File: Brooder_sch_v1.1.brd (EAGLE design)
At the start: 80 x 75 mm, 28 parts, among them J1 DCJ0202, U1 328P

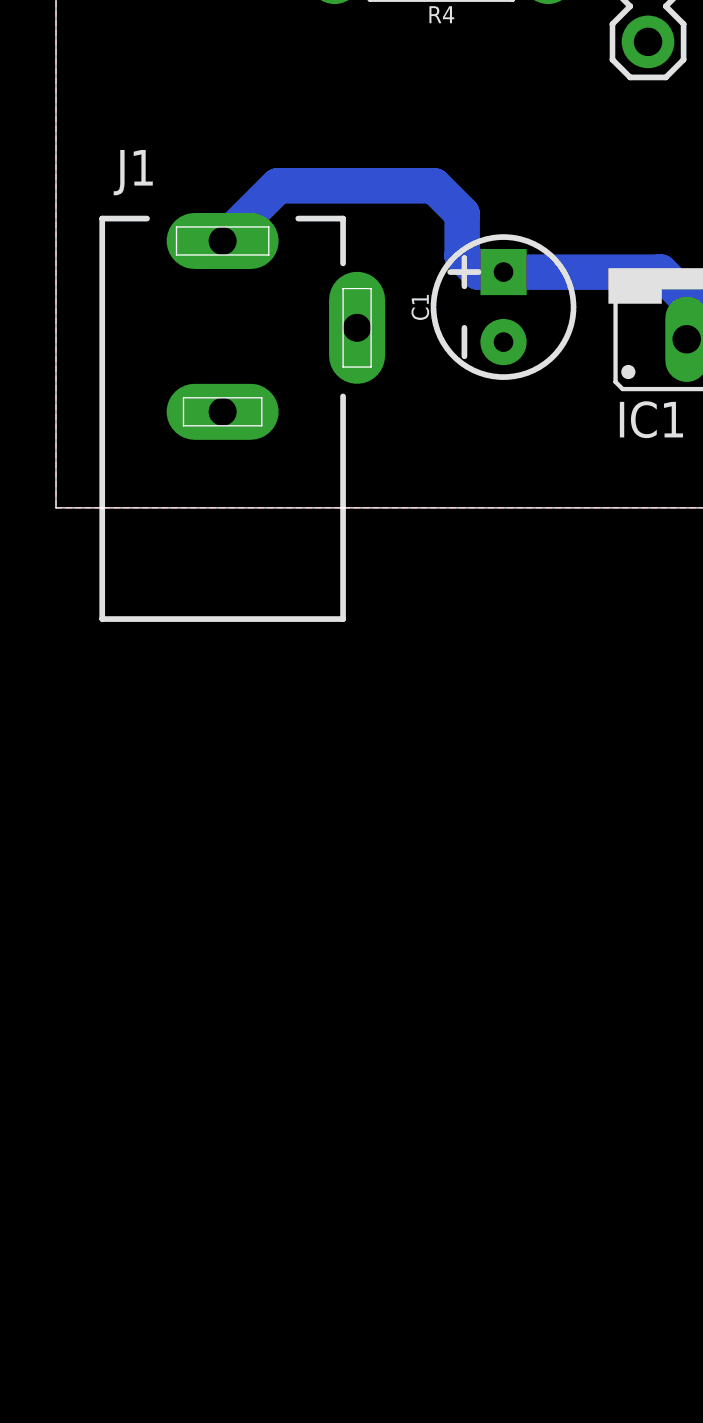
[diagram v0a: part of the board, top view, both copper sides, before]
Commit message: Adds space for the rocker switch
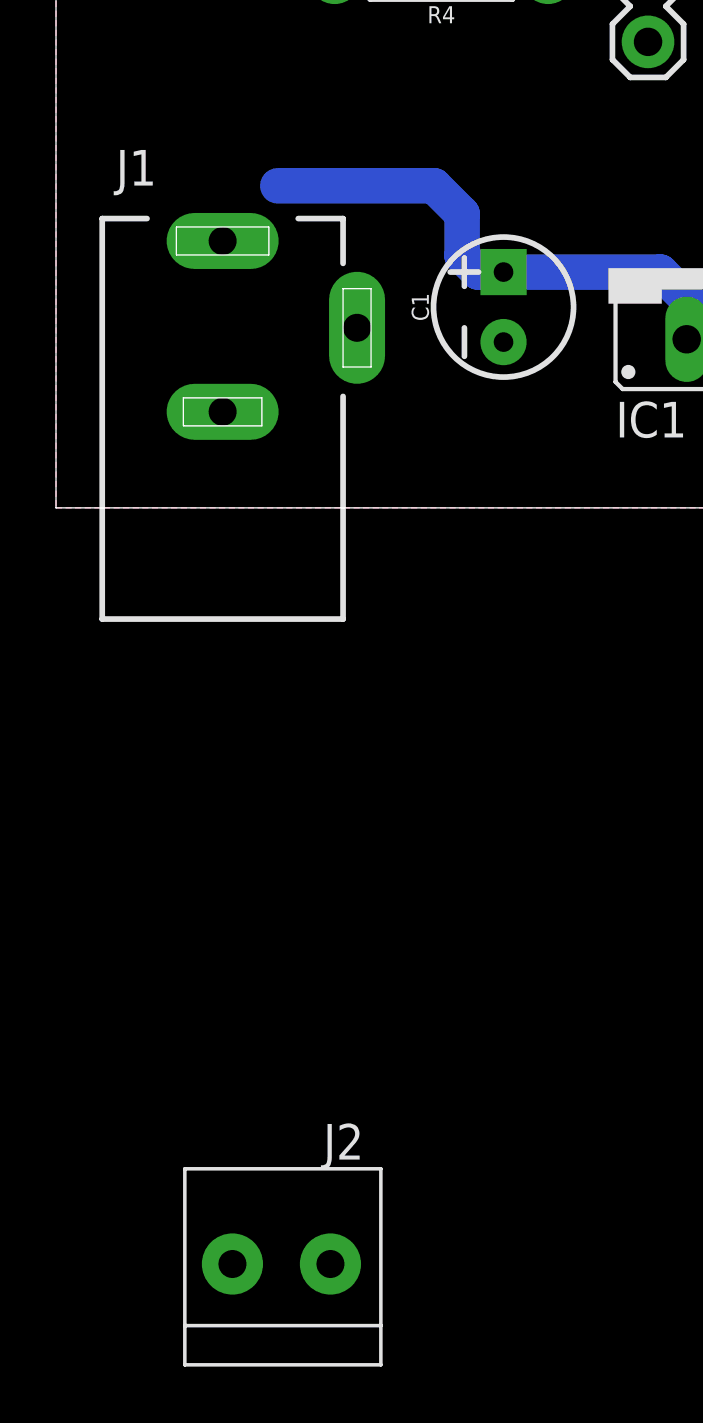
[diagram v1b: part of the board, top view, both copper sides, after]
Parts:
- added J2: 1X2-3.5MM, adafruit:1X2-3.5MM
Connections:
- new net 12V_S: C1.1, IC1.IN, J2.2
- net 12V: now also J2.1; no longer C1.1, IC1.IN
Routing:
- net 12V: track 21.4 -> 0.00 mm
- net 12V_S: track 0.00 -> 18.6 mm
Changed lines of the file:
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@@
 <attribute name="PROD_ID" value="IC-09136" x="38.13" y="40.02" size="1.778" layer="27" rot="R270" display="off"/>
 </element>
+<element name="J2" library="adafruit" package="1X2-3.5MM" value="1X2-3.5MM" x="8" y="-27"/>
 </elements>
 <signals>
@@
 <signal name="12V">
 <contactref element="J1" pad="1"/>
-<contactref element="C1" pad="1"/>
-<contactref element="IC1" pad="IN"/>
-<wire x1="5.95" y1="9.53" x2="7.92" y2="11.5" width="1.27" layer="16"/>
-<wire x1="7.92" y1="11.5" x2="13.5" y2="11.5" width="1.27" layer="16"/>
-<wire x1="13.5" y1="11.5" x2="14.5" y2="10.5" width="1.27" layer="16"/>
-<wire x1="14.5" y1="10.5" x2="14.5" y2="9" width="1.27" layer="16"/>
-<wire x1="14.5" y1="9" x2="15.08" y2="8.42" width="1.27" layer="16"/>
-<wire x1="15.08" y1="8.42" x2="15.98" y2="8.42" width="1.27" layer="16"/>
-<wire x1="15.98" y1="8.42" x2="21.58" y2="8.42" width="1.27" layer="16"/>
-<wire x1="22.52" y1="7.48" x2="22.52" y2="6.02" width="1.27" layer="16"/>
-<wire x1="21.58" y1="8.42" x2="22.52" y2="7.48" width="1.27" layer="16"/>
+<contactref element="J2" pad="1"/>
+<wire x1="5.95" y1="9.53" x2="9.8" y2="-27" width="0" layer="19" extent="1-1"/>
 </signal>
 <signal name="5V">
@@
 <wire x1="41.99" y1="26" x2="41.94" y2="26.05" width="1.27" layer="16"/>
 </signal>
+<signal name="12V_S">
+<contactref element="C1" pad="1"/>
+<contactref element="IC1" pad="IN"/>
+<contactref element="J2" pad="2"/>
+<wire x1="7.92" y1="11.5" x2="13.5" y2="11.5" width="1.27" layer="16"/>
+<wire x1="13.5" y1="11.5" x2="14.5" y2="10.5" width="1.27" layer="16"/>
+<wire x1="14.5" y1="10.5" x2="14.5" y2="9" width="1.27" layer="16"/>
+<wire x1="14.5" y1="9" x2="15.08" y2="8.42" width="1.27" layer="16"/>
+<wire x1="15.08" y1="8.42" x2="15.98" y2="8.42" width="1.27" layer="16"/>
+<wire x1="15.98" y1="8.42" x2="21.58" y2="8.42" width="1.27" layer="16"/>
+<wire x1="22.52" y1="7.48" x2="22.52" y2="6.02" width="1.27" layer="16"/>
+<wire x1="21.58" y1="8.42" x2="22.52" y2="7.48" width="1.27" layer="16"/>
+<wire x1="15.08" y1="8.42" x2="6.3" y2="-27" width="0" layer="19" extent="16-16"/>
+</signal>
 </signals>

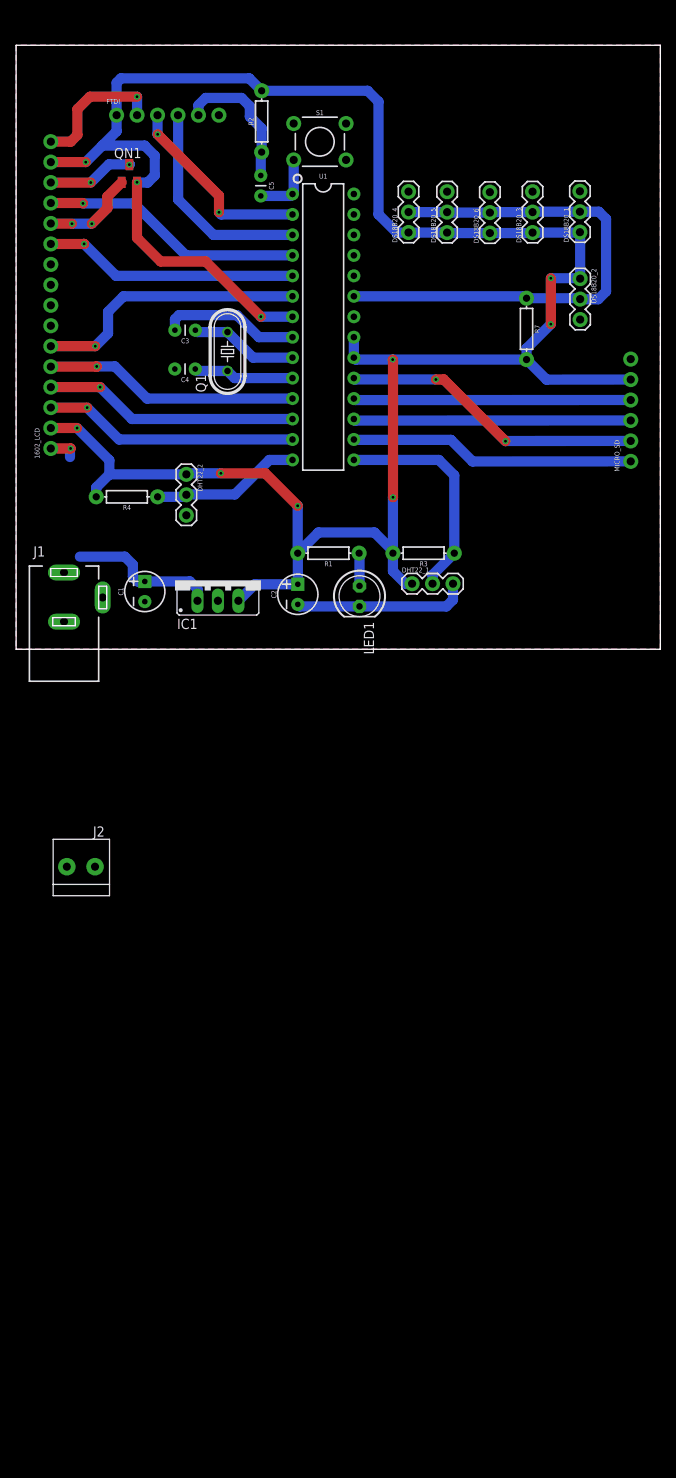
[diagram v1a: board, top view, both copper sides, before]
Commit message: Resolves inconsistencies between the board and schematic
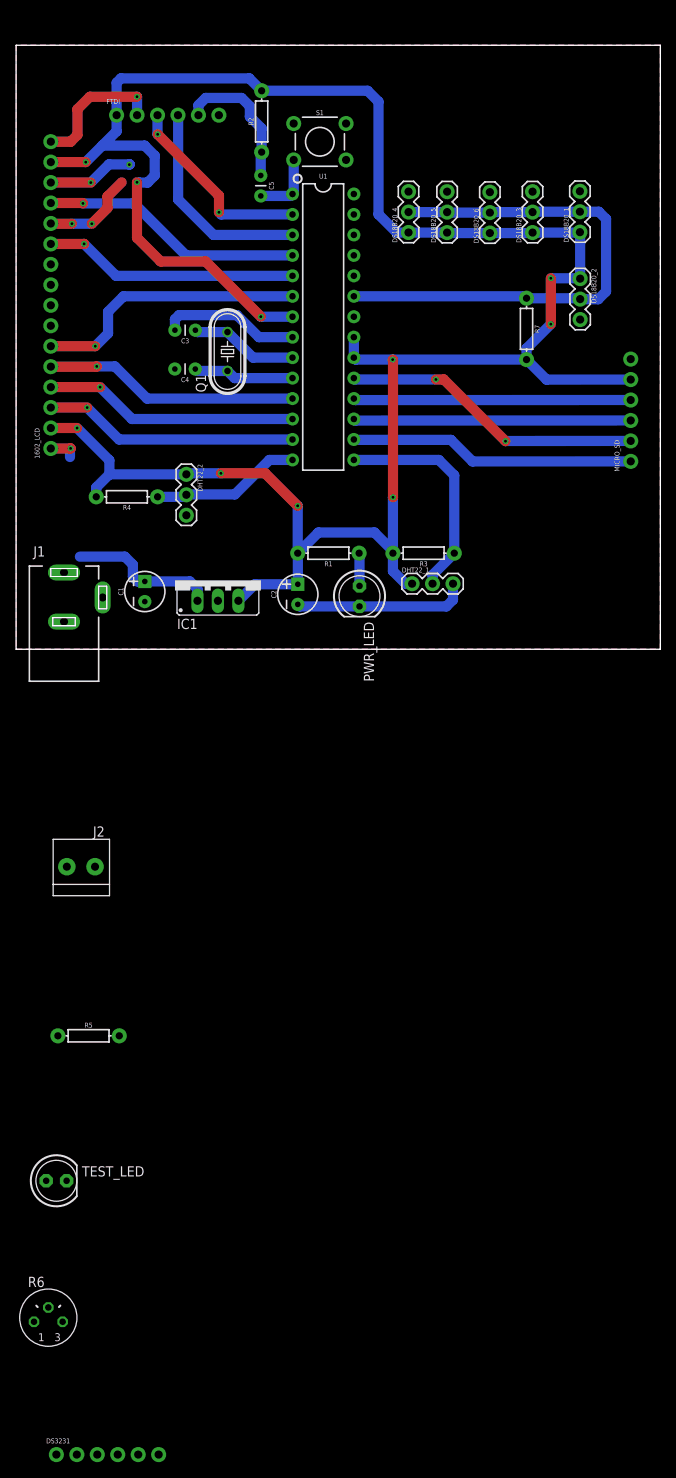
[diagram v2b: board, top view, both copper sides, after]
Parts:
- removed QN1: (no value), sym:SOT23
- added DS3231: (no value), SparkFun-Connectors:1X06_NO_SILK
- added R5: 220, SparkFun-Resistors:AXIAL-0.3
- added R6: (no value), pot:RJ6
- added TEST_LED: (no value), adafruit:LED5MM
- renumbered LED1 to PWR_LED
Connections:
- new net N$1: R5.P$1, TEST_LED.A
- new net PC1: R5.P$2, U1.24
- new net PC4: DS3231.4, U1.27
- new net PC5: DS3231.3, U1.28
- net 5V: now also DS3231.5, R6.E; no longer QN1.2
- net GND: now also DS3231.6, R6.A, TEST_LED.K; no longer QN1.1
- net VO: now also R6.S; no longer QN1.3
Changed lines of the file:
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@@
 <attribute name="OC_NEWARK" value="unknown" x="5.95" y="6.43" size="1.778" layer="27" display="off"/>
 </element>
-<element name="LED1" library="adafruit" package="LED5MM" value="" x="42.64" y="6.59" rot="R270"/>
+<element name="PWR_LED" library="adafruit" package="LED5MM" value="" x="42.64" y="6.59" rot="R270"/>
 <element name="MICRO_SD" library="SparkFun-Connectors" package="1X06_NO_SILK" value="" x="76.32" y="23.33" rot="R90">
 <attribute name="PROD_ID" value="CONN-08437" x="76.32" y="23.33" size="1.778" layer="27" rot="R90" display="off"/>
@@
 <attribute name="OC_NEWARK" value="unknown" x="26.25" y="36.97" size="1.778" layer="27" rot="R90" display="off"/>
 </element>
-<element name="QN1" library="sym" package="SOT23" value="" x="14.06" y="59.08"/>
 <element name="R1" library="SparkFun-Resistors" package="AXIAL-0.3" value="220" x="38.78" y="11.93" rot="R180">
 <attribute name="PROD_ID" value="RES-09327" x="38.78" y="11.93" size="1.778" layer="27" rot="R180" display="off"/>
@@
 </element>
 <element name="J2" library="adafruit" package="1X2-3.5MM" value="1X2-3.5MM" x="8" y="-27"/>
+<element name="R5" library="SparkFun-Resistors" package="AXIAL-0.3" value="220" x="9" y="-48">
+<attribute name="PROD_ID" value="RES-09327" x="9" y="-48" size="1.778" layer="27" display="off"/>
+</element>
+<element name="TEST_LED" library="adafruit" package="LED5MM" value="" x="5" y="-66"/>
+<element name="R6" library="pot" library_urn="urn:adsk.eagle:library:331" package="RJ6" package3d_urn="urn:adsk.eagle:package:22699/1" value="" x="4" y="-83"/>
+<element name="DS3231" library="SparkFun-Connectors" package="1X06_NO_SILK" value="" x="5" y="-100">
+<attribute name="PROD_ID" value="CONN-08437" x="5" y="-100" size="1.778" layer="27" display="off"/>
+</element>
 </elements>
 <signals>
@@
 <contactref element="IC1" pad="GND"/>
 <contactref element="C2" pad="2"/>
-<contactref element="LED1" pad="K"/>
+<contactref element="PWR_LED" pad="K"/>
 <contactref element="S1" pad="1"/>
 <contactref element="C3" pad="2"/>
@@
 <contactref element="1602_LCD" pad="12"/>
 <contactref element="1602_LCD" pad="1"/>
-<contactref element="QN1" pad="1"/>
 <contactref element="MICRO_SD" pad="6"/>
 <contactref element="DS18B20_3" pad="3"/>
@@
 <vertex x="0" y="75"/>
 </polygon>
+<contactref element="TEST_LED" pad="K"/>
+<contactref element="R6" pad="A"/>
+<contactref element="DS3231" pad="6"/>
+<wire x1="64.13" y1="56.82" x2="70.01" y2="56.87" width="0" layer="19" extent="1-1"/>
+<wire x1="58.83" y1="56.76" x2="64.13" y2="56.82" width="0" layer="19" extent="1-1"/>
+<wire x1="53.52" y1="56.82" x2="58.83" y2="56.76" width="0" layer="19" extent="1-1"/>
+<wire x1="48.73" y1="56.83" x2="53.52" y2="56.82" width="0" layer="19" extent="1-1"/>
+<wire x1="70.04" y1="40.94" x2="70.01" y2="56.87" width="0" layer="19" extent="1-1"/>
+<wire x1="76.32" y1="36.03" x2="70.04" y2="40.94" width="0" layer="19" extent="1-1"/>
+<wire x1="34.4688" y1="65.2806" x2="48.73" y2="56.83" width="0" layer="19" extent="1-1"/>
+<wire x1="41.94" y1="41.29" x2="48.73" y2="56.83" width="0" layer="19" extent="1-1"/>
+<wire x1="34.32" y1="38.75" x2="41.94" y2="41.29" width="0" layer="19" extent="1-1"/>
+<wire x1="19.71" y1="34.8" x2="19.72" y2="39.62" width="0" layer="19" extent="1-1"/>
+<wire x1="9.4" y1="52.84" x2="20.24" y2="41.49" width="0" layer="19" extent="1-16"/>
+<wire x1="7.61" y1="63.85" x2="13.11" y2="57.98" width="0" layer="19" extent="1-1"/>
+<wire x1="6.77" y1="24.94" x2="19.71" y2="34.8" width="0" layer="19" extent="16-16"/>
+<wire x1="21.14" y1="16.64" x2="6.69" y2="23.87" width="0" layer="19" extent="16-16"/>
+<wire x1="25.06" y1="6.02" x2="21.14" y2="16.64" width="0" layer="19" extent="1-1"/>
+<wire x1="15.98" y1="5.92" x2="25.06" y2="6.02" width="0" layer="19" extent="1-1"/>
+<wire x1="10.75" y1="6.43" x2="15.98" y2="5.92" width="0" layer="19" extent="1-1"/>
+<wire x1="5.95" y1="3.43" x2="10.75" y2="6.43" width="0" layer="19" extent="1-1"/>
+<wire x1="34.98" y1="5.57" x2="25.06" y2="6.02" width="0" layer="19" extent="1-1"/>
+<wire x1="6.27" y1="-66" x2="5.95" y2="3.43" width="0" layer="19" extent="1-1"/>
+<wire x1="2.222" y1="-83.508" x2="6.27" y2="-66" width="0" layer="19" extent="1-1"/>
+<wire x1="17.7" y1="-100" x2="2.222" y2="-83.508" width="0" layer="19" extent="1-1"/>
 </signal>
 <signal name="12V">
@@
 <contactref element="1602_LCD" pad="15"/>
 <contactref element="1602_LCD" pad="2"/>
-<contactref element="QN1" pad="2"/>
 <contactref element="MICRO_SD" pad="5"/>
 <contactref element="DS18B20_3" pad="1"/>
@@
 <wire x1="13.02" y1="70.89" x2="28.95" y2="70.89" width="1.27" layer="16"/>
 <wire x1="28.95" y1="70.89" x2="30.49" y2="69.35" width="1.27" layer="16"/>
+<contactref element="R6" pad="E"/>
+<contactref element="DS3231" pad="5"/>
+<wire x1="5.778" y1="-83.508" x2="15.16" y2="-100" width="0" layer="19" extent="1-1"/>
+<wire x1="27.6" y1="6.02" x2="5.778" y2="-83.508" width="0" layer="19" extent="1-1"/>
 </signal>
 <signal name="N$3">
 <contactref element="R1" pad="P$1"/>
-<contactref element="LED1" pad="A"/>
+<contactref element="PWR_LED" pad="A"/>
 <wire x1="42.59" y1="11.93" x2="42.64" y2="11.88" width="1.27" layer="16"/>
 <wire x1="42.64" y1="11.88" x2="42.64" y2="7.86" width="1.27" layer="16"/>
@@
 <signal name="VO">
 <contactref element="1602_LCD" pad="14"/>
-<contactref element="QN1" pad="3"/>
 <wire x1="11.53" y1="60.21" x2="14.09" y2="60.21" width="1.27" layer="16"/>
 <wire x1="14.1" y1="60.21" x2="14.09" y2="60.21" width="1.27" layer="16"/>
@@
 <wire x1="4.31" y1="57.95" x2="9.27" y2="57.95" width="1.27" layer="1"/>
 <via x="9.27" y="57.95" extent="1-16" drill="0.35"/>
+<contactref element="R6" pad="S"/>
+<wire x1="4.31" y1="57.95" x2="4" y2="-81.73" width="0" layer="19" extent="1-1"/>
 </signal>
 <signal name="PD2">
@@
 <wire x1="15.08" y1="8.42" x2="6.3" y2="-27" width="0" layer="19" extent="16-16"/>
 </signal>
+<signal name="N$1">
+<contactref element="R5" pad="P$1"/>
+<contactref element="TEST_LED" pad="A"/>
+<wire x1="5.19" y1="-48" x2="3.73" y2="-66" width="0" layer="19" extent="1-1"/>
+</signal>
+<signal name="PC1">
+<contactref element="U1" pad="24"/>
+<contactref element="R5" pad="P$2"/>
+<wire x1="12.81" y1="-48" x2="41.94" y2="46.37" width="0" layer="19" extent="1-1"/>
+</signal>
+<signal name="PC4">
+<contactref element="DS3231" pad="4"/>
+<contactref element="U1" pad="27"/>
+<wire x1="12.62" y1="-100" x2="41.94" y2="53.99" width="0" layer="19" extent="1-1"/>
+</signal>
+<signal name="PC5">
+<contactref element="DS3231" pad="3"/>
+<contactref element="U1" pad="28"/>
+<wire x1="10.08" y1="-100" x2="41.94" y2="56.53" width="0" layer="19" extent="1-1"/>
+</signal>
 </signals>
-<errors>
-</errors>
 </board>
 </drawing>

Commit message: Completes redesign of the board
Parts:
- moved DS3231 167.9 mm to (49.0, 62.0), turned to 270 degrees
- moved R6 142.4 mm to (14.0, 59.0), turned to 90 degrees
- moved TEST_LED 114.6 mm to (51.0, 39.0)
- moved R5 97.9 mm to (45.0, 43.0), turned to 90 degrees
- moved J2 35.4 mm to (16.6, 7.37), turned to 180 degrees
- moved DS18B20_1 27.2 mm to (47.2, 66.7)
- moved DS18B20_4 22.1 mm to (65.0, 66.7)
- moved DS18B20_3 18.1 mm to (74.4, 66.7)
- moved R3 17.1 mm to (67.6, 9.93)
- moved R1 17.0 mm to (55.8, 10.9)
- moved DHT22_1 16.1 mm to (65.2, 6.14)
- moved DS18B20_5 15.1 mm to (55.8, 66.7)
- moved PWR_LED 13.8 mm to (56.4, 5.64), turned to 0 degrees
- moved C2 11.0 mm to (46.0, 6.82)
- moved IC1 10.0 mm to (35.1, 8.56)
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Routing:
- net 5V: track 291.6 -> 347.7 mm, vias 10 -> 8
- net PC0: track 65.9 -> 91.2 mm
- net PB1: track 27.8 -> 43.1 mm
- net 12V: track 0.00 -> 13.3 mm
- net PC5: track 0.00 -> 7.22 mm
- net PC4: track 0.00 -> 7.22 mm
- net N$1: track 0.00 -> 4.81 mm
- net N$3: track 4.09 -> 8.75 mm
- net GND: track 71.5 -> 76.0 mm, vias 4 -> 3
- net 12V_S: track 18.6 -> 14.8 mm
- net PC1: track 0.00 -> 3.24 mm
- net N$4: track 8.33 -> 11.3 mm
- net VO: track 10.8 -> 8.85 mm, vias 2 -> 1
- net PB4: track 34.5 -> 35.7 mm
- net PB3: track 34.5 -> 35.7 mm
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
